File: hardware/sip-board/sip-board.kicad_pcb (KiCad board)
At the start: 8 copper layers, 17 x 50 mm, 85 parts, among them IC1 XC7S15-1CPGA196C, J1 Conn_01x06_Pin, J2 Conn_01x10_Pin, J3 Conn_01x10_Pin, J4 Conn_01x10_Pin, J5 Conn_01x10_Pin, SW1 SW_DIP_x03, SW2 SW_RESET, U1 TLV75718PDRV, U2 TLV75733PDRV, U3 TLV75710PDRV, U4 M95256-WMN6P

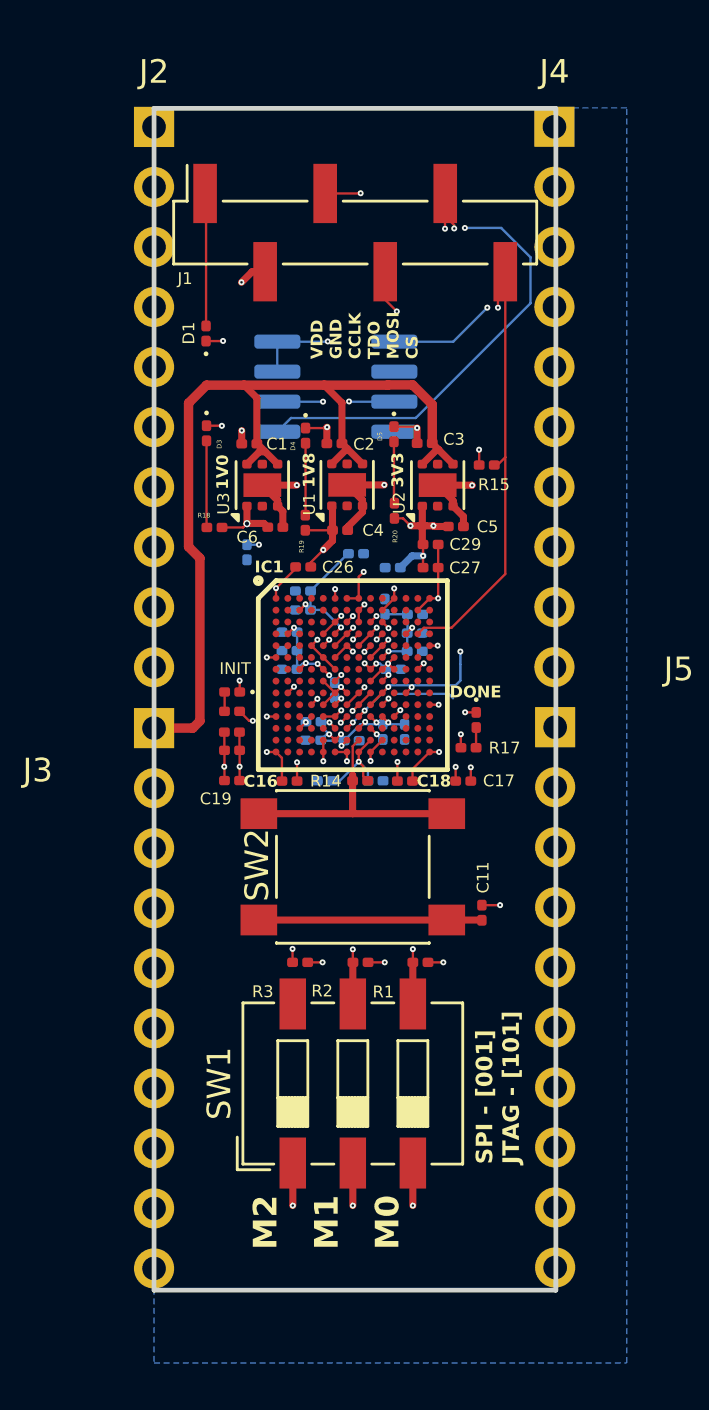
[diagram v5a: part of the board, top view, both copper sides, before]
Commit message: pinout labels
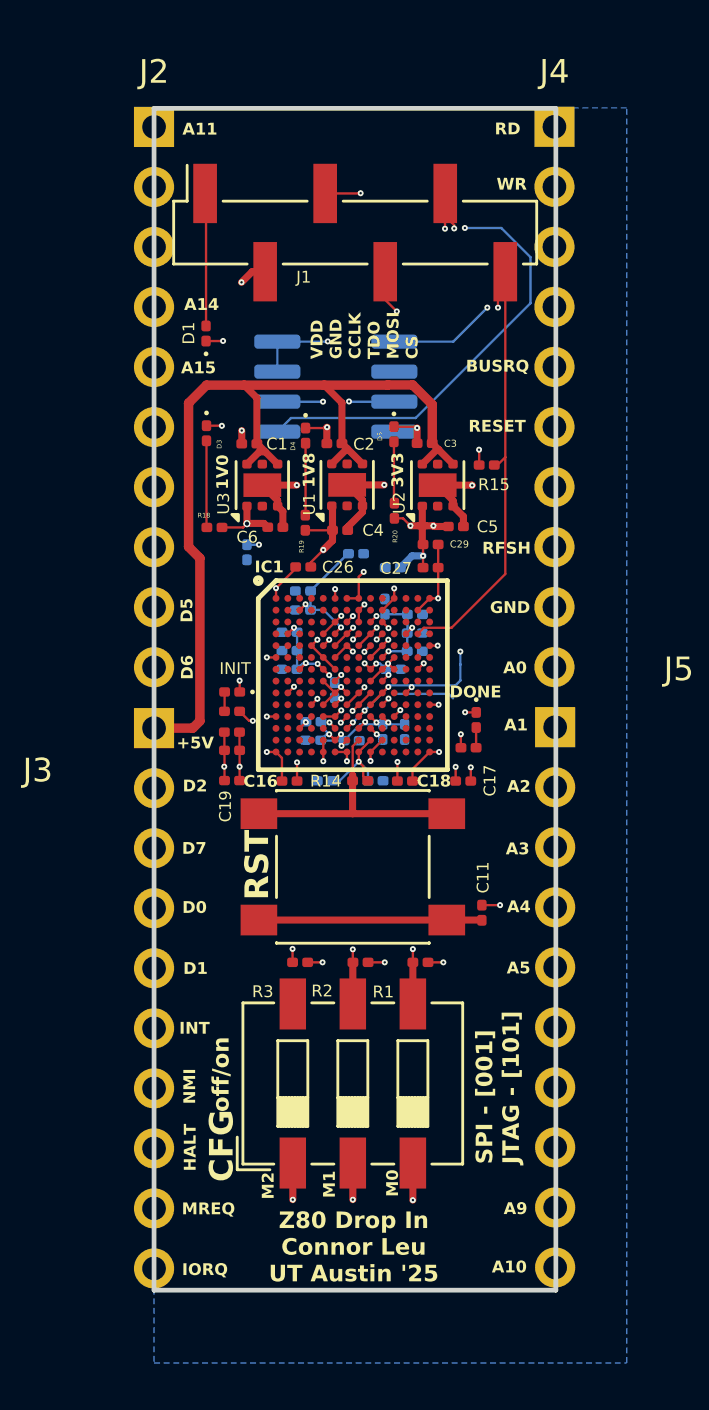
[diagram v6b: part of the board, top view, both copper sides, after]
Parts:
- renumbered SW1 to CFG, SW2 to RST
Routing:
- net +3V3: track 39.6 -> 38.9 mm
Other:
- board text added: "+5V"
- board text added: "A0"
- board text added: "A1"
- board text added: "A10"
- board text added: "A11"
- board text added: "A12"
- board text added: "A13"
- board text added: "A14"
- board text added: "A15"
- board text added: "A2"
- board text added: "A3"
- board text added: "A4"
- board text added: "A5"
- board text added: "A6"
- board text added: "A7"
- board text added: "A8"
- board text added: "A9"
- board text added: "BUSAK"
- board text added: "BUSRQ"
- board text added: "CLK"
- board text added: "D0"
- board text added: "D1"
- board text added: "D2"
- board text added: "D3"
- board text added: "D4"
- board text added: "D5"
- board text added: "D6"
- board text added: "D7"
- board text added: "GND"
- board text added: "HALT"
- board text added: "INT"
- board text added: "IORQ"
- board text added: "MREQ"
- board text added: "NMI"
- board text added: "RD"
- board text added: "RESET"
- board text added: "RFSH"
- board text added: "WAIT"
- board text added: "WR"
- board text added: "Z80 Drop In Connor Leu UT Austin '25"
- board text added: "off/on"

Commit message: some cleanup
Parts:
- R10, R11, R12, R13, R4, R5, R6, R7, R8, R9, U10, U11, U12, U13, U14, U5, U6, U7, U8, U9: moved to B.Cu
- moved R13 41.0 mm to (151.4, 120.7), turned to -90 degrees
- moved U9 39.6 mm to (139.9, 125.8), turned to 180 degrees
- moved U10 39.0 mm to (150.6, 80.9)
- moved R9 38.7 mm to (151.1, 80.0), turned to -90 degrees
- moved U14 38.6 mm to (151.0, 122.1)
- moved R12 37.7 mm to (151.4, 110.4), turned to -90 degrees
- moved R8 36.9 mm to (139.5, 126.9), turned to 90 degrees
- moved R10 36.6 mm to (151.3, 90.6), turned to -90 degrees
- moved R11 36.4 mm to (151.3, 102.6), turned to -90 degrees
- moved U11 34.4 mm to (150.9, 92.0)
- moved U13 34.1 mm to (151.0, 111.9)
- moved U12 33.1 mm to (150.8, 103.7)
- moved U8 31.4 mm to (139.9, 115.0), turned to 180 degrees
- moved R7 31.2 mm to (139.5, 115.7), turned to 90 degrees
- moved R4 28.6 mm to (140.0, 85.7), turned to 90 degrees
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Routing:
- net +5V: track 40.4 -> 132.3 mm, vias 0 -> 12
- net +3V3: track 38.9 -> 64.7 mm, vias 22 -> 41
- net DIN: track 0.00 -> 11.0 mm, vias 0 -> 2
- net WAIT_5V: track 0.00 -> 7.00 mm, vias 0 -> 1
- net BUSRQ_5V: track 0.00 -> 6.51 mm, vias 0 -> 1
- net A10_5V: track 0.00 -> 6.46 mm, vias 0 -> 1
- net A3_5V: track 0.00 -> 6.25 mm, vias 0 -> 1
- net A6_5V: track 0.00 -> 5.98 mm, vias 0 -> 1
- net A7_5V: track 0.00 -> 5.87 mm, vias 0 -> 1
- net RD_5V: track 0.00 -> 5.72 mm, vias 0 -> 1
- net RFSH_5V: track 0.00 -> 5.70 mm, vias 0 -> 1
- net A11_5V: track 0.00 -> 4.95 mm
- net A0_5V: track 0.00 -> 4.91 mm
- net BUSAK_5V: track 0.00 -> 4.90 mm, vias 0 -> 1
- net NMI_5V: track 0.00 -> 4.60 mm
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
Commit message: files
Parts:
- renumbered DONE to D2, INIT to D6, CFG to SW1, RST to SW2
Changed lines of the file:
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@@
 		(descr "LED SMD 0201 (0603 Metric), square (rectangular) end terminal, IPC_7351 nominal, (Body size source: https://www.vishay.com/docs/20052/crcw0201e3.pdf), generated with kicad-footprint-generator")
 		(tags "LED")
-		(property "Reference" "INIT"
+		(property "Reference" "D6"
 			(at -0.125 0.99 180)
 			(layer "F.SilkS")
@@
 		(descr "LED SMD 0201 (0603 Metric), square (rectangular) end terminal, IPC_7351 nominal, (Body size source: https://www.vishay.com/docs/20052/crcw0201e3.pdf), generated with kicad-footprint-generator")
 		(tags "LED")
-		(property "Reference" "DONE"
+		(property "Reference" "D2"
 			(at -1.185 0.03 180)
 			(layer "F.SilkS")
@@
 		(sheetname "Root")
 		(sheetfile "sip-board.kicad_sch")
-		(attr through_hole)
+		(attr through_hole exclude_from_bom dnp)
 		(fp_line
 			(start -1.8 -1.8)
@@
 		(sheetname "Root")
 		(sheetfile "sip-board.kicad_sch")
-		(attr through_hole)
+		(attr through_hole exclude_from_bom dnp)
 		(fp_line
 			(start -1.8 -1.8)
@@
 		(descr "SMD 3x-dip-switch SPST , Slide, row spacing 6.73 mm (264 mils), body size 6.7x9.18mm (see e.g. https://www.ctscorp.com/wp-content/uploads/219.pdf), SMD, LowProfile, JPin")
 		(tags "SMD DIP Switch SPST Slide 6.73mm 264mil SMD LowProfile JPin")
-		(property "Reference" "CFG"
+		(property "Reference" "SW1"
 			(at -2.635 -5.55 -90)
 			(layer "F.SilkS")
@@
 		(sheetname "Root")
 		(sheetfile "sip-board.kicad_sch")
-		(attr through_hole)
+		(attr through_hole exclude_from_bom dnp)
 		(fp_line
 			(start -1.8 -1.8)
@@
 		(sheetname "Root")
 		(sheetfile "sip-board.kicad_sch")
-		(attr through_hole)
+		(attr through_hole exclude_from_bom dnp)
 		(fp_line
 			(start -1.8 -1.8)
@@
 		(descr "tactile push button, 6x6mm e.g. PTS645xx series, height=9.5mm")
 		(tags "tact sw push 6mm smd")
-		(property "Reference" "RST"
+		(property "Reference" "SW2"
 			(at -4.05 -0.08 90)
 			(layer "F.SilkS")
